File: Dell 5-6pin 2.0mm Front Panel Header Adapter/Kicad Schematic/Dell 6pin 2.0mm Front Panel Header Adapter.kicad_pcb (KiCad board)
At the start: 2 copper layers, 17.2 x 14 mm, 2 parts, among them J1 Dell Connector, J2 2.54mm Panel Header

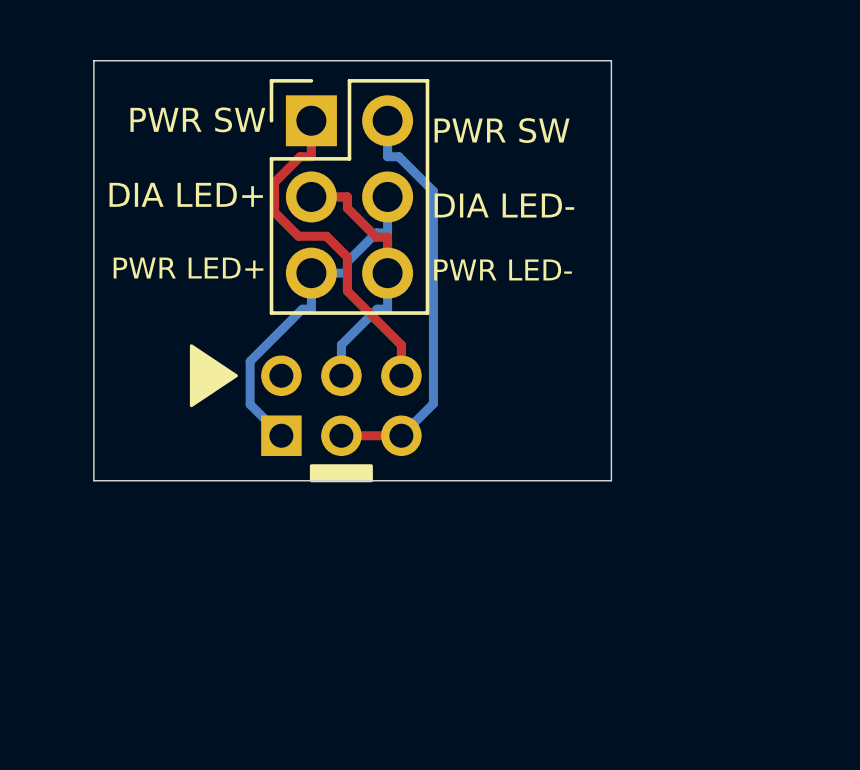
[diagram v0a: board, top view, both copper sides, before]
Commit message: redesign PCB to fit (more) Micro ATX cases
The original PCB hung off the side of the motherboard.
If the motherboard is mounted very close to the power
supply, the PCB won't physically fit.

One example of a case with this issue is the Rosewill
LINE-M.

The redesigned PCB should (hopefully) not hang off
edge of the motherboard at all.  I don't believe it
will physically obstruct any other connector, but I
haven't had it fabbed yet, so we'll see.
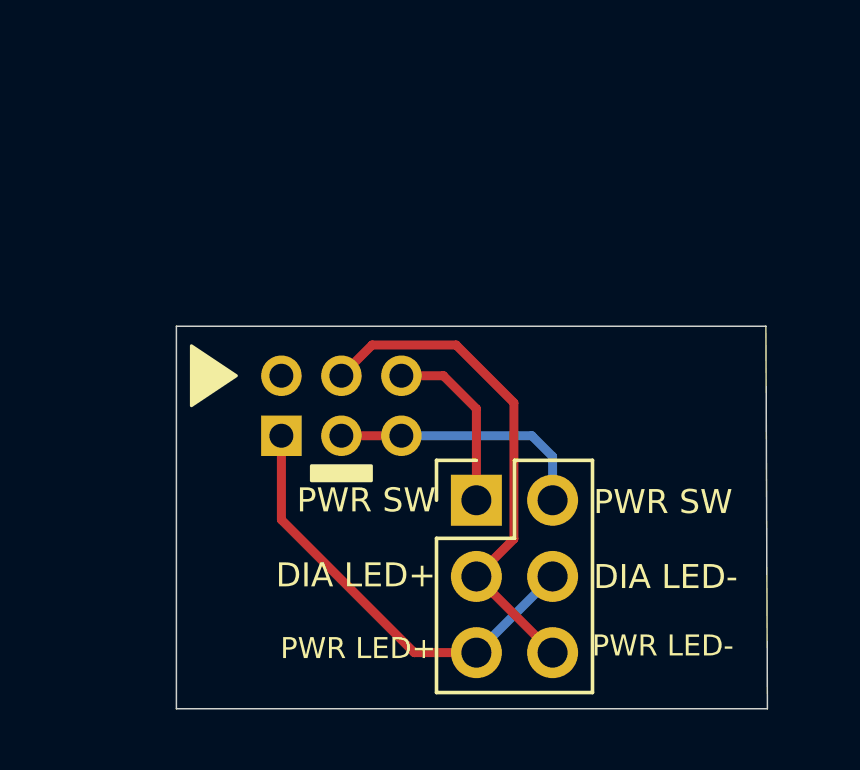
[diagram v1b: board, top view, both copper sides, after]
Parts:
- moved J2 13.8 mm to (166.0, 101.2)
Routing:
- net DIAGNOSTIC_LED+: track 8.77 -> 16.9 mm
- net POWER_SW_A: track 11.5 -> 6.01 mm
- net POWER_SW_B: track 13.8 -> 8.79 mm
- net DIAGNOSTIC_LED-: track 11.4 -> 14.7 mm
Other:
- board size 17.2 x 14 mm -> 19.7 x 12.8 mm
- board text added: "daveho mod Feb 2022 github.com/daveho"
